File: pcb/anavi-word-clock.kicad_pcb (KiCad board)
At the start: 2 copper layers, 65.3 x 32.8 mm, 17 parts, among them J1 Conn_01x04_Female, J2 Conn_01x04_Female, J3 Conn_01x04_Female, J5 Conn_01x04_Male, J7 Screw_Terminal_01x03, U1 XIAO ESP32C3, U2 74LVC1G17W5-7

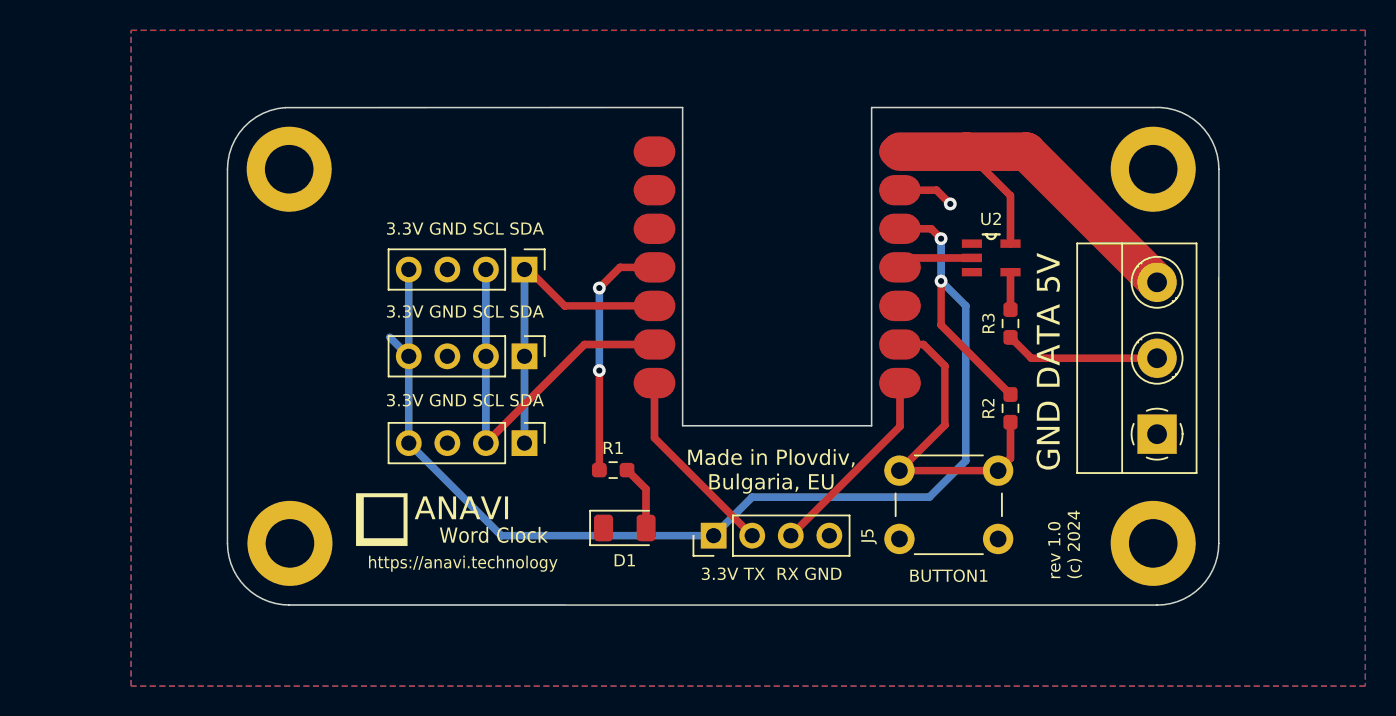
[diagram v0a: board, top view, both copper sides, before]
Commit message: pcb: Change the PCB design
Update the schematics and change the PCB design to support I2C RTC
module with 1x6 female connector.

Signed-off-by: Leon Anavi <leon@anavi.org>
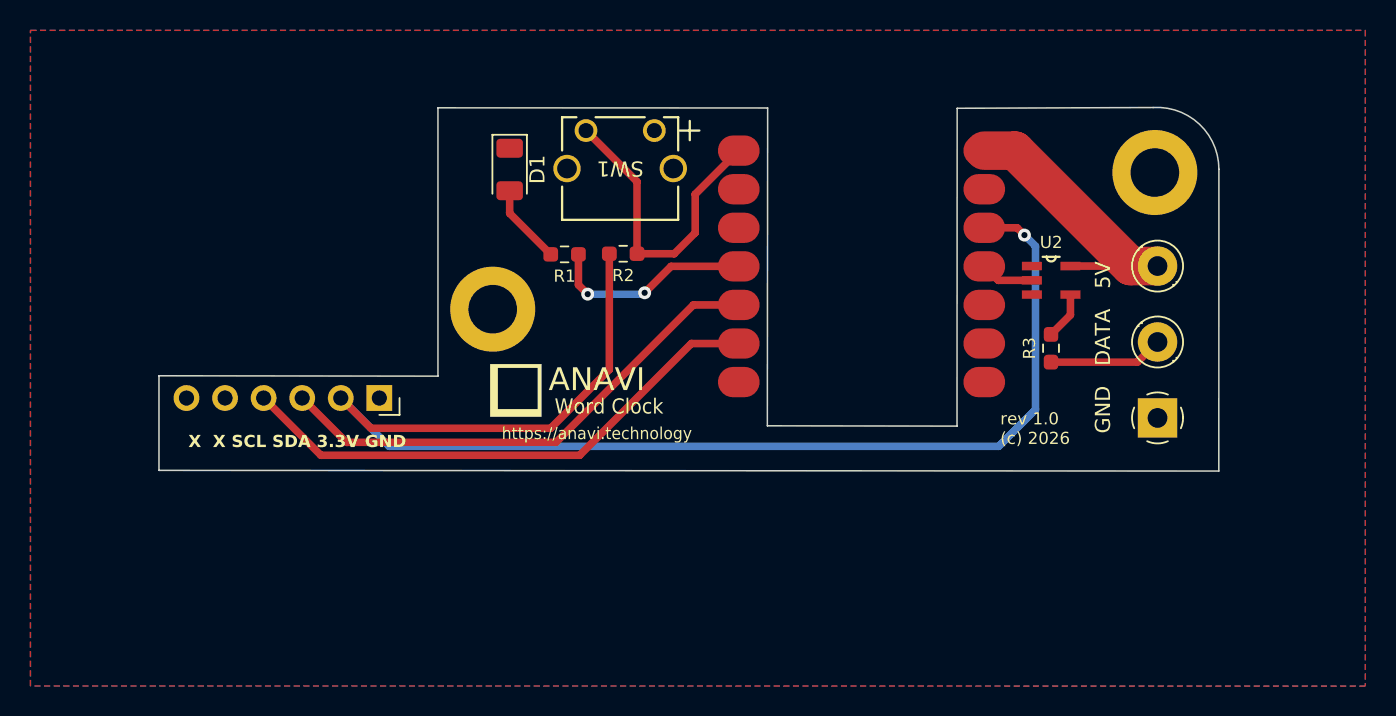
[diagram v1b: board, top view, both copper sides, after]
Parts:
- removed BUTTON1: SW_DIP_x01, Button_Switch_THT:SW_PUSH_6mm_H4.3mm
- removed J2, J3: Conn_01x04_Female, Connector_PinHeader_2.54mm:PinHeader_1x04_P2.54mm_Vertical
- removed J5: Conn_01x04_Male, Connector_PinHeader_2.54mm:PinHeader_1x04_P2.54mm_Vertical
- removed the REF** at (117.1, 61.7)
- removed the REF** at (174.0, 61.7)
- added SW1: SW_DIP_x01, TL1105SF160Q:SW_TL1105SF160Q_EWI, F.Cu at (141.1, 34.5)
- D1: value KP-3216EC -> LED
- J1: value Conn_01x04_Female -> Conn_01x06; footprint Connector_PinHeader_2.54mm:PinHeader_1x04_P2.54mm_Vertical -> Connector_PinSocket_2.54mm:PinSocket_1x06_P2.54mm_Horizontal
- U1: value XIAO ESP32C3 -> MOUDLE-SEEEDUINO-XIAO-ESP32C3
- moved R2 27.5 mm to (139.1, 42.6), turned to 180 degrees
- moved D1 24.8 mm to (131.6, 37.1), turned to -90 degrees
- moved REF** 16.3 mm to (130.5, 46.3)
- moved R1 14.6 mm to (135.2, 42.7), turned to 180 degrees
- moved G*** 12.3 mm to (132.0, 51.7)
- moved J1 10.0 mm to (123.0, 52.1)
- moved U1 5.55 mm to (145.9, 54.0)
- moved U2 4.21 mm to (167.3, 44.4)
- moved R3 3.13 mm to (167.3, 48.9)
- moved J7 1.07 mm to (174.3, 53.5)
- moved REF** 0.24 mm to (174.1, 37.3)
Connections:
- J1 pad 1: Net-(J1-Pad1) -> GND
- J1 pad 2: Net-(J1-Pad2) -> +3.3V
- J1 pad 3: GND -> Net-(J1-Pin_3)
- J1 pad 4: +3V3 -> Net-(J1-Pin_4)
- R2 pad 1: Net-(R2-Pad1) -> Net-(U1-PA02_A0_D0)
- R2 pad 2: +3V3 -> +3.3V
- U1 pad 1: Net-(J6-Pad1) -> Net-(U1-PA02_A0_D0)
- U1 pad 12: +3V3 -> +3.3V
- U1 pad 2: Net-(J6-Pad2) -> unconnected-(U1-PA4_A1_D1-Pad2)
- U1 pad 3: Net-(J6-Pad3) -> unconnected-(U1-PA10_A2_D2-Pad3)
- U1 pad 5: Net-(J1-Pad1) -> Net-(J1-Pin_3)
- U1 pad 6: Net-(J1-Pad2) -> Net-(J1-Pin_4)
- U1 pad 7: Net-(J5-Pad2) -> unconnected-(U1-PB08_A6_D6_TX-Pad7)
- U1 pad 8: Net-(J5-Pad3) -> unconnected-(U1-PB09_A7_D7_RX-Pad8)
- U1 pad 9: Net-(R2-Pad1) -> unconnected-(U1-PA7_A8_D8_SCK-Pad9)
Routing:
- net +3.3V: track 0.00 -> 90.4 mm, vias 0 -> 1
- net +3V3: track 82.1 -> 0.00 mm, vias 2 -> 0
- net Net-(J1-Pin_4): track 0.00 -> 35.9 mm
- net Net-(J1-Pin_3): track 0.00 -> 33.7 mm
- net Net-(J1-Pad2): track 25.2 -> 0.00 mm
- net Net-(R2-Pad1): track 21.7 -> 0.00 mm
- net Net-(J1-Pad1): track 21.0 -> 0.00 mm
- net Net-(U1-PA02_A0_D0): track 0.00 -> 20.5 mm
- net Net-(J5-Pad3): track 13.0 -> 0.00 mm
- net Net-(J5-Pad2): track 12.7 -> 0.00 mm
- net +5V: track 27.8 -> 18.5 mm
- net GND: track 3.69 -> 0.00 mm, vias 1 -> 0
- net Net-(J7-Pin_2): track 10.2 -> 7.56 mm
- net Net-(U1-PA11_A3_D3): track 16.2 -> 13.6 mm
- net Net-(U1-PA6_A10_D10_MOSI): track 4.99 -> 3.52 mm
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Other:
- board size 65.3 x 32.8 mm -> 69.8 x 23.9 mm
- board text added: "X X SCL SDA 3.3V GND"
- board text added: "rev 1.0 (c) 2026"
- board text removed: "3.3V GND SCL SDA"
- board text removed: "3.3V TX RX GND"
- board text removed: "rev 1.0 (c) 2024"

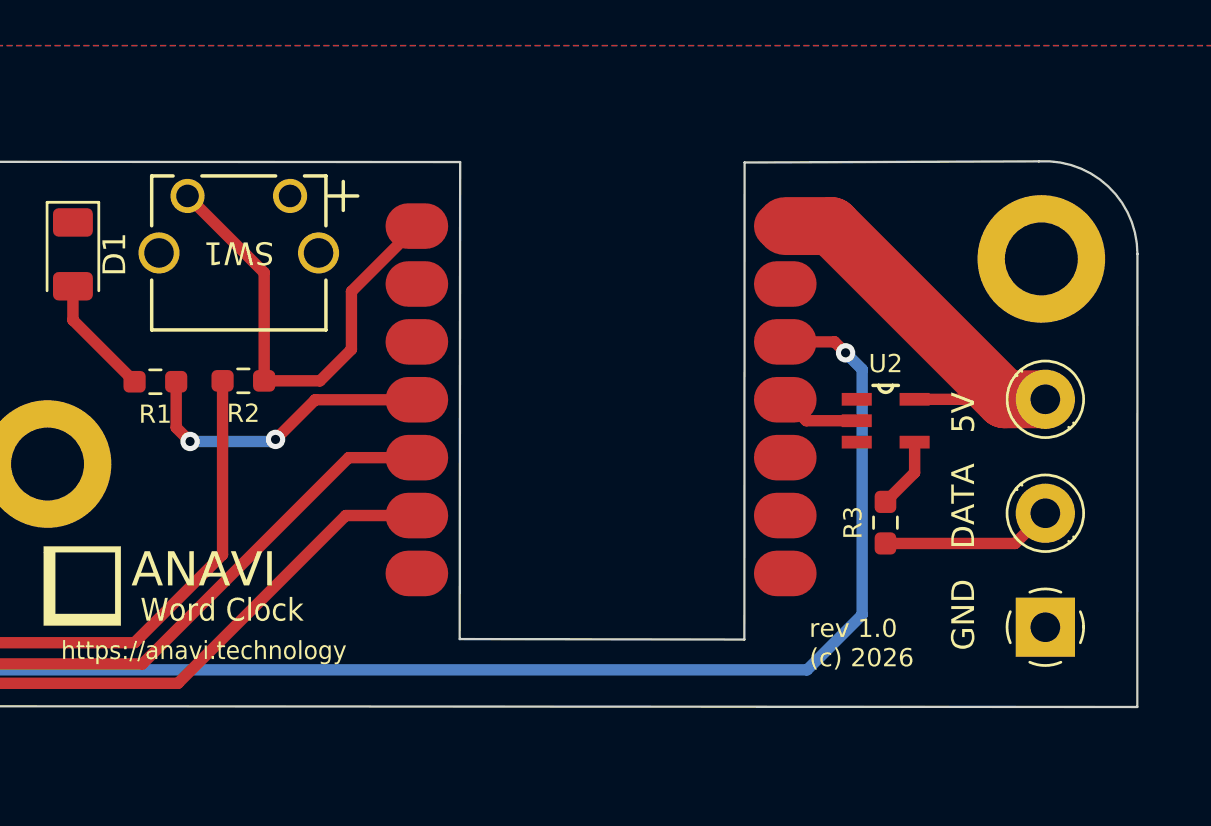
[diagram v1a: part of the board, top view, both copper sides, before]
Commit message: pcb: Use XIAO ESP32C6
Switch the footprint from XIAO ESP32C3 to ESP32C6 because of the
on-board antenna with up to 80m BLE/Wi-Fi range which makes the
assembly of the clock easier.

Signed-off-by: Leon Anavi <leon@anavi.org>
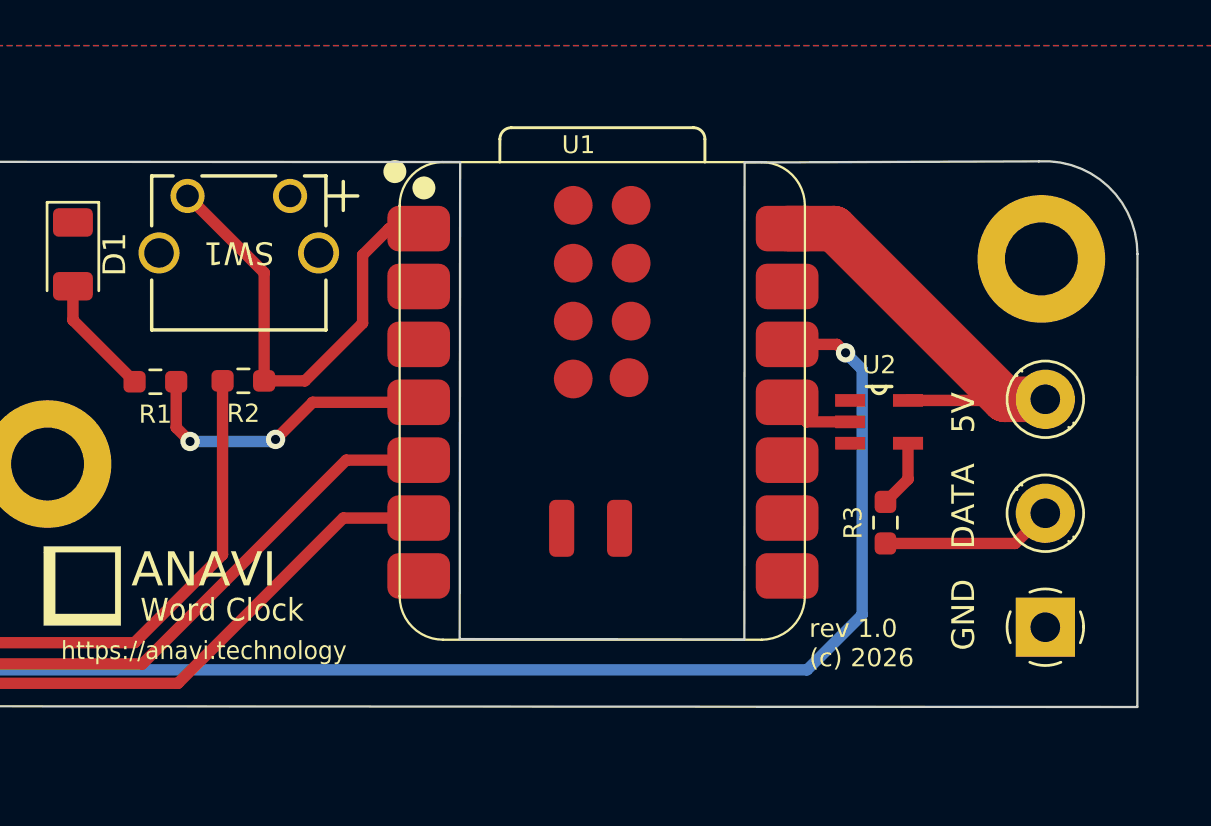
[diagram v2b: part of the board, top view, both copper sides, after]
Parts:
- U1: value MOUDLE-SEEEDUINO-XIAO-ESP32C3 -> XIAO ESP32C6; footprint xiao ESP32C3_PCB:MOUDLE14P-SMD-2.54-21X17.8MM -> xiao-esp32c6:XIAO-ESP32-C6-SMD
- moved U2 0.29 mm to (167.0, 44.4)
- moved U1 0.14 mm to (145.9, 54.1)
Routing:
- net +5V: track 18.5 -> 20.5 mm

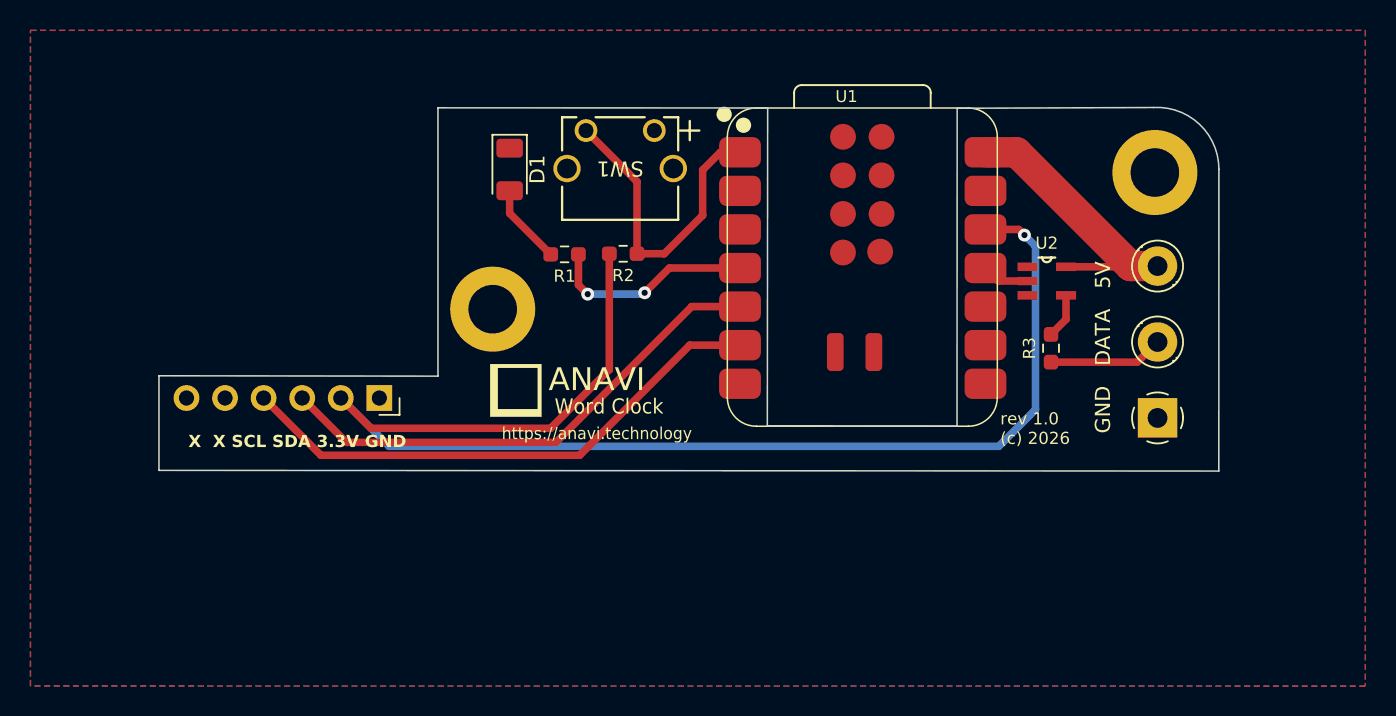
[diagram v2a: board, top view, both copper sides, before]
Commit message: pcb: anavi-word-clock.kicad_pcb: Fix errors
Fix DRC errors and warnings.

Signed-off-by: Leon Anavi <leon@anavi.org>
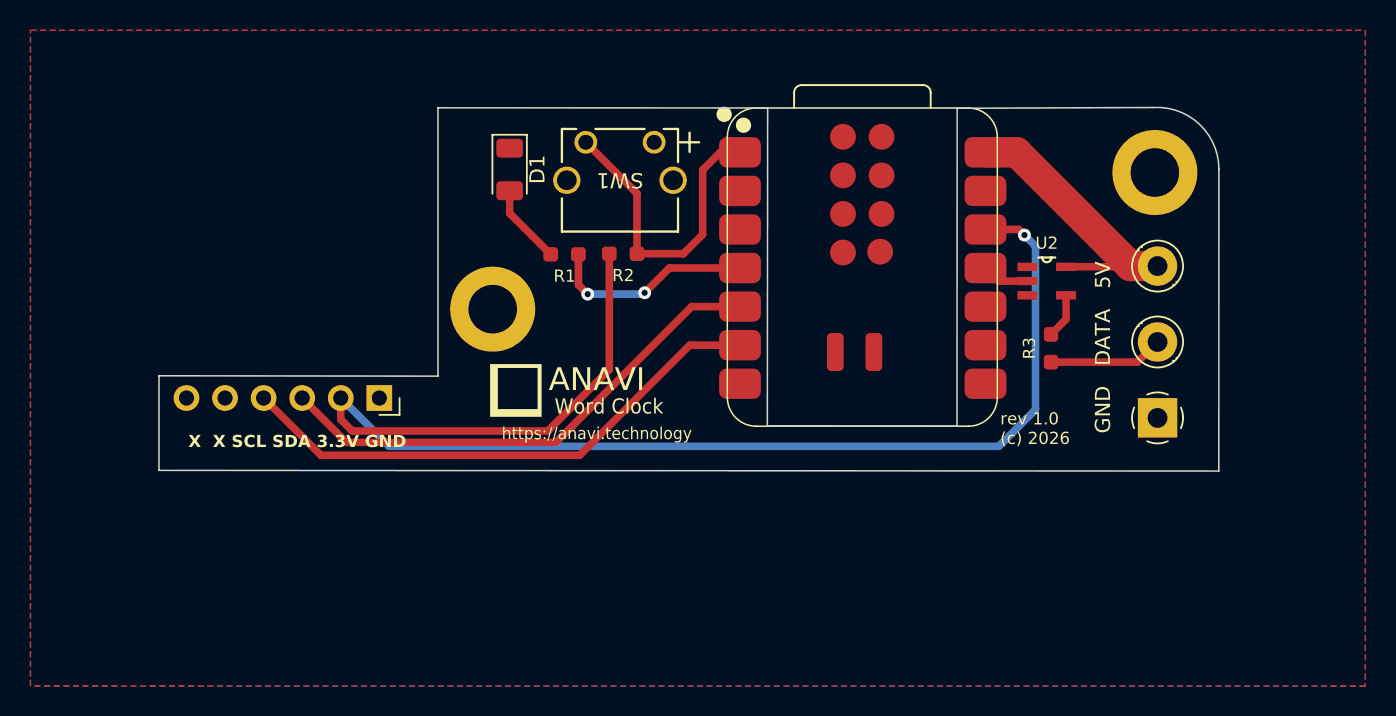
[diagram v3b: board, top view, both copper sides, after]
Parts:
- moved SW1 0.77 mm to (141.1, 35.3)
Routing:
- net +3.3V: track 90.3 -> 91.3 mm
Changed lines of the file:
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@@
 		(sheetname "/")
 		(sheetfile "anavi-word-clock.kicad_sch")
-		(units
-			(unit
-				(name "A")
-				(pins "1" "2")
-			)
-		)
 		(attr smd)
 		(duplicate_pad_numbers_are_jumpers no)
-		(fp_line
-			(start -0.254724 0.5225)
-			(end 0.254724 0.5225)
-			(stroke
-				(width 0.12)
-				(type solid)
-			)
-			(layer "F.SilkS")
-		)
-		(fp_line
-			(start -0.254724 -0.5225)
-			(end 0.254724 -0.5225)
-			(stroke
-				(width 0.12)
-				(type solid)
-			)
-			(layer "F.SilkS")
-		)
 		(fp_rect
 			(start -1.65 -0.73)
@@
 		(sheetname "/")
 		(sheetfile "anavi-word-clock.kicad_sch")
-		(units
-			(unit
-				(name "A")
-				(pins "1" "2")
-			)
-		)
 		(attr smd)
 		(duplicate_pad_numbers_are_jumpers no)
-		(fp_line
-			(start -0.254724 0.5225)
-			(end 0.254724 0.5225)
-			(stroke
-				(width 0.12)
-				(type solid)
-			)
-			(layer "F.SilkS")
-		)
-		(fp_line
-			(start -0.254724 -0.5225)
-			(end 0.254724 -0.5225)
-			(stroke
-				(width 0.12)
-				(type solid)
-			)
-			(layer "F.SilkS")
-		)
 		(fp_rect
 			(start -1.65 -0.73)
@@
 		(sheetname "/")
 		(sheetfile "anavi-word-clock.kicad_sch")
-		(units
-			(unit
-				(name "A")
-				(pins "1" "2" "3" "4" "5" "6")
-			)
-		)
 		(attr through_hole)
 		(duplicate_pad_numbers_are_jumpers no)
@@
 			(at 7.112 -21.336 0)
 			(layer "F.SilkS")
+			(hide yes)
 			(effects
 				(font
@@
 		(layer "F.Cu")
 		(at 174.1 37.3)
-		(descr "Mounting Hole 3.2mm, M3, DIN965")
-		(tags "mounting hole 3.2mm m3 din965")
+		(descr "Mounting Hole 3.2mm, M3, generated by kicad-footprint-generator mountinghole.py")
+		(tags "mountinghole M3 DIN965")
 		(property "Reference" "REF**"
 			(at 0 -3.8 0)
@@
 			)
 		)
+		(property "KiLib_Generator" "mounting_hardware/mounting_hole"
+			(at 0 0 0)
+			(layer "F.SilkS")
+			(hide yes)
+			(effects
+				(font
+					(size 1 1)
+					(thickness 0.15)
+				)
+			)
+		)
 		(property "Field4" "${REFERENCE}"
 			(at 0 0 0)
@@
 			(layer "F.CrtYd")
 		)
+		(fp_text user "${REFERENCE}"
+			(at 0 0 0)
+			(layer "F.Fab")
+			(effects
+				(font
+					(size 1 1)
+					(thickness 0.15)
+				)
+			)
+		)
 		(pad "2" thru_hole circle
 			(at 0 0)
@@
 			(layers "*.Cu" "*.Mask")
 			(remove_unused_layers no)
+			(zone_connect 2)
 		)
 		(embedded_fonts no)
@@
 	(footprint "TL1105SF160Q:SW_TL1105SF160Q_EWI"
 		(layer "F.Cu")
-		(at 141.137501 34.5375 180)
+		(at 141.125166 35.309999 180)
 		(tags "TL1105SF160Q ")
 		(property "Reference" "SW1"
@@
 		(sheetname "/")
 		(sheetfile "anavi-word-clock.kicad_sch")
-		(units
-			(unit
-				(name "A")
-				(pins "5" "2" "1" "3" "4")
-			)
-		)
 		(attr smd)
 		(duplicate_pad_numbers_are_jumpers no)
@@
 			(pinfunction "NC_1")
 			(pintype "no_connect")
+			(solder_mask_margin 0.05)
+			(solder_paste_margin 0.05)
+			(clearance 0.1)
 		)
 		(pad "2" smd rect
@@
 			(pinfunction "A_2")
 			(pintype "input")
+			(solder_mask_margin 0.05)
+			(solder_paste_margin 0.05)
+			(clearance 0.1)
 		)
 		(pad "3" smd rect
@@
 			(pinfunction "GND_3")
 			(pintype "passive")
+			(solder_mask_margin 0.05)
+			(solder_paste_margin 0.05)
+			(clearance 0.1)
 		)
 		(pad "4" smd rect
@@
 			(pinfunction "Y_4")
 			(pintype "output")
+			(solder_mask_margin 0.05)
+			(solder_paste_margin 0.05)
+			(clearance 0.1)
 		)
 		(pad "5" smd rect
@@
 			(pinfunction "VCC_5")
 			(pintype "power_in")
+			(solder_mask_margin 0.05)
+			(solder_paste_margin 0.05)
+			(clearance 0.1)
 		)
 		(embedded_fonts no)
@@
 		)
 		(property "KiLib_Generator" "SMD_2terminal_chip_molded"
-			(at 0 0 270)
+			(at 0 0 90)
 			(layer "F.SilkS")
 			(hide yes)
@@
 		(sheetname "/")
 		(sheetfile "anavi-word-clock.kicad_sch")
-		(units
-			(unit
-				(name "A")
-				(pins "1" "2")
-			)
-		)
 		(attr smd)
 		(duplicate_pad_numbers_are_jumpers no)
-		(fp_line
-			(start -0.254724 0.5225)
-			(end 0.254724 0.5225)
-			(stroke
-				(width 0.12)
-				(type solid)
-			)
-			(layer "F.SilkS")
-		)
-		(fp_line
-			(start -0.254724 -0.5225)
-			(end 0.254724 -0.5225)
-			(stroke
-				(width 0.12)
-				(type solid)
-			)
-			(layer "F.SilkS")
-		)
 		(fp_rect
 			(start -1.65 -0.73)
@@
 	)
 	(segment
-		(start 140 37.9)
+		(start 140 38.684834)
 		(end 140 42.65)
 		(width 0.5)
@@
 	)
 	(segment
-		(start 140 42.65)
-		(end 141.79 42.65)
+		(start 143.05 42.65)
+		(end 140 42.65)
 		(width 0.5)
 		(layer "F.Cu")
@@
 	)
 	(segment
-		(start 144.32 37.13)
-		(end 145.48 35.97)
+		(start 144.32 41.38)
+		(end 143.05 42.65)
 		(width 0.5)
 		(layer "F.Cu")
@@
 	)
 	(segment
-		(start 141.79 42.65)
-		(end 144.32 40.12)
+		(start 144.32 37.13)
+		(end 144.32 41.38)
 		(width 0.5)
 		(layer "F.Cu")
@@
 	)
 	(segment
-		(start 144.32 40.12)
+		(start 145.48 35.97)
 		(end 144.32 37.13)
 		(width 0.5)
@@
 	)
 	(segment
-		(start 145.48 35.97)
-		(end 146.78 35.97)
+		(start 146.78 35.97)
+		(end 145.48 35.97)
 		(width 0.5)
 		(layer "F.Cu")
@@
 	)
 	(segment
-		(start 136.6375 34.5375)
-		(end 140 37.9)
+		(start 136.625165 35.309999)
+		(end 140 38.684834)
 		(width 0.5)
 		(layer "F.Cu")
@@
 	)
 	(segment
-		(start 162.945 41.05)
-		(end 165.14 41.05)
+		(start 121.25 54.32)
+		(end 134.13 54.32)
 		(width 0.5)
 		(layer "F.Cu")
@@
 	)
 	(segment
-		(start 138.175 50.275)
-		(end 134.31 54.14)
+		(start 120.490114 53.560114)
+		(end 121.25 54.32)
+		(width 0.5)
+		(layer "F.Cu")
+		(net "+3.3V")
+	)
+	(segment
+		(start 162.945 41.05)
+		(end 165.14 41.05)
 		(width 0.5)
 		(layer "F.Cu")
@@
 	)
 	(segment
-		(start 122.480114 54.14)
-		(end 120.490114 52.15)
+		(start 138.175 50.275)
+		(end 138.175 42.65)
 		(width 0.5)
 		(layer "F.Cu")
@@
 	)
 	(segment
-		(start 134.31 54.14)
-		(end 122.480114 54.14)
+		(start 134.13 54.32)
+		(end 138.175 50.275)
 		(width 0.5)
 		(layer "F.Cu")
@@
 	)
 	(segment
-		(start 138.175 42.65)
-		(end 138.175 50.275)
+		(start 120.490114 52.15)
+		(end 120.490114 53.560114)
 		(width 0.5)
 		(layer "F.Cu")
@@
 		(layer "F.Cu")
 		(hatch edge 0.508)
+		(priority 1)
 		(connect_pads
-			(clearance 0.508)
+			(clearance 0.1524)
 		)
 		(min_thickness 0.254)
@@
 			(thermal_bridge_width 0.508)
 			(island_removal_mode 0)
-			(hatch_thickness 1)
-			(hatch_gap 1)
+			(hatch_thickness 0.5)
+			(hatch_gap 0.5)
 			(hatch_orientation 0)
 			(hatch_border_algorithm hatch_thickness)
@@
 		(hatch edge 0.508)
 		(connect_pads
-			(clearance 0.508)
+			(clearance 0.1524)
 		)
 		(min_thickness 0.254)
@@
 			(thermal_bridge_width 0.508)
 			(island_removal_mode 0)
-			(hatch_thickness 1)
-			(hatch_gap 1)
+			(hatch_thickness 0.5)
+			(hatch_gap 0.5)
 			(hatch_orientation 0)
 			(hatch_border_algorithm hatch_thickness)
